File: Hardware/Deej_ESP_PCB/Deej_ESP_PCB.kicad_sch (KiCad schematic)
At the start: 1 part, among them U1 ESP32-S3-MINI-1U

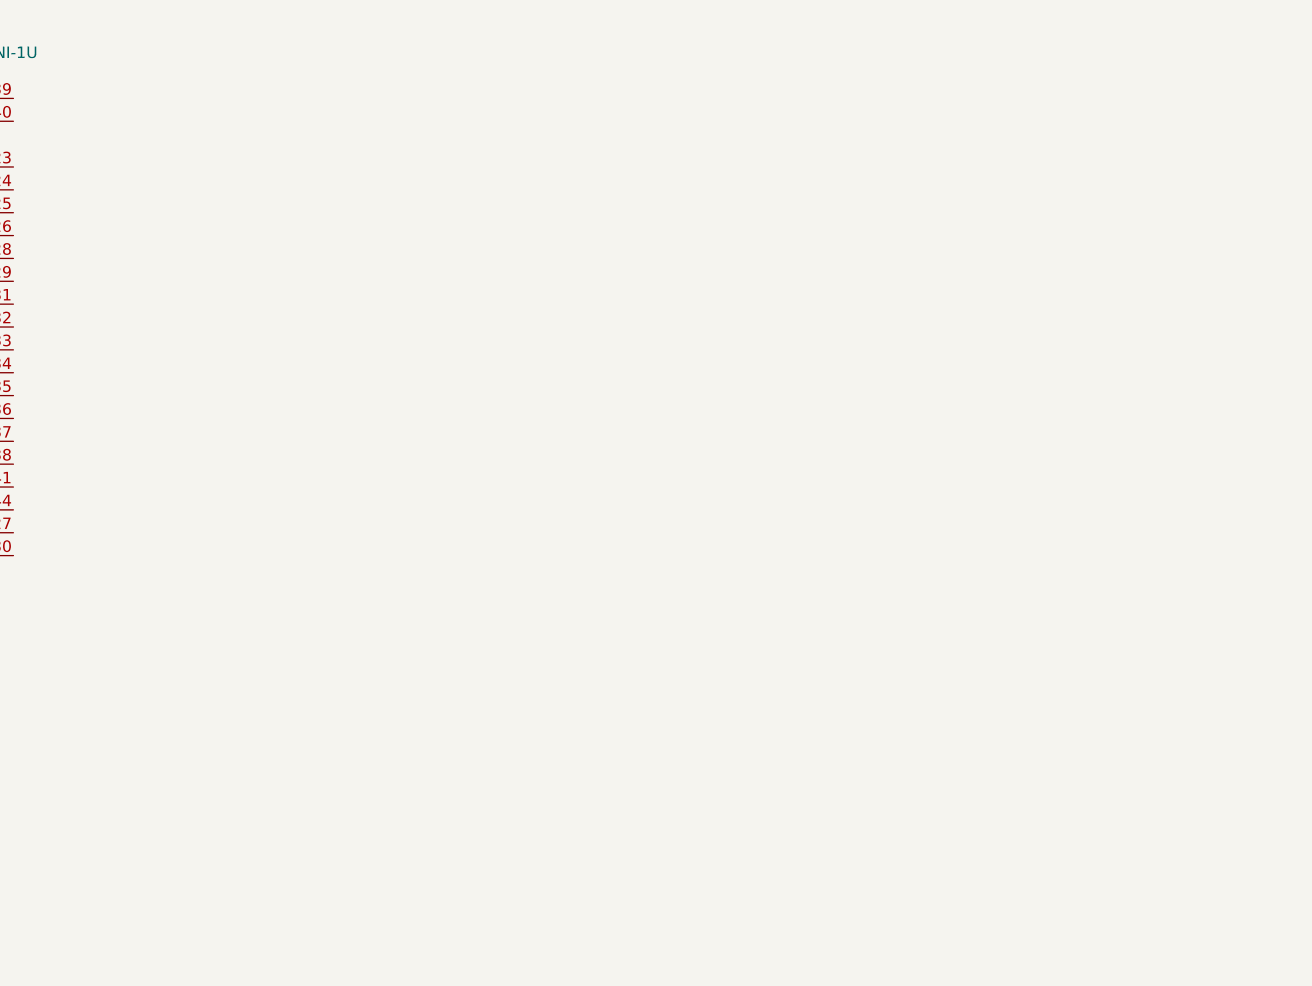
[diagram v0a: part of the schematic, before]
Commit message: Adding components to the part library
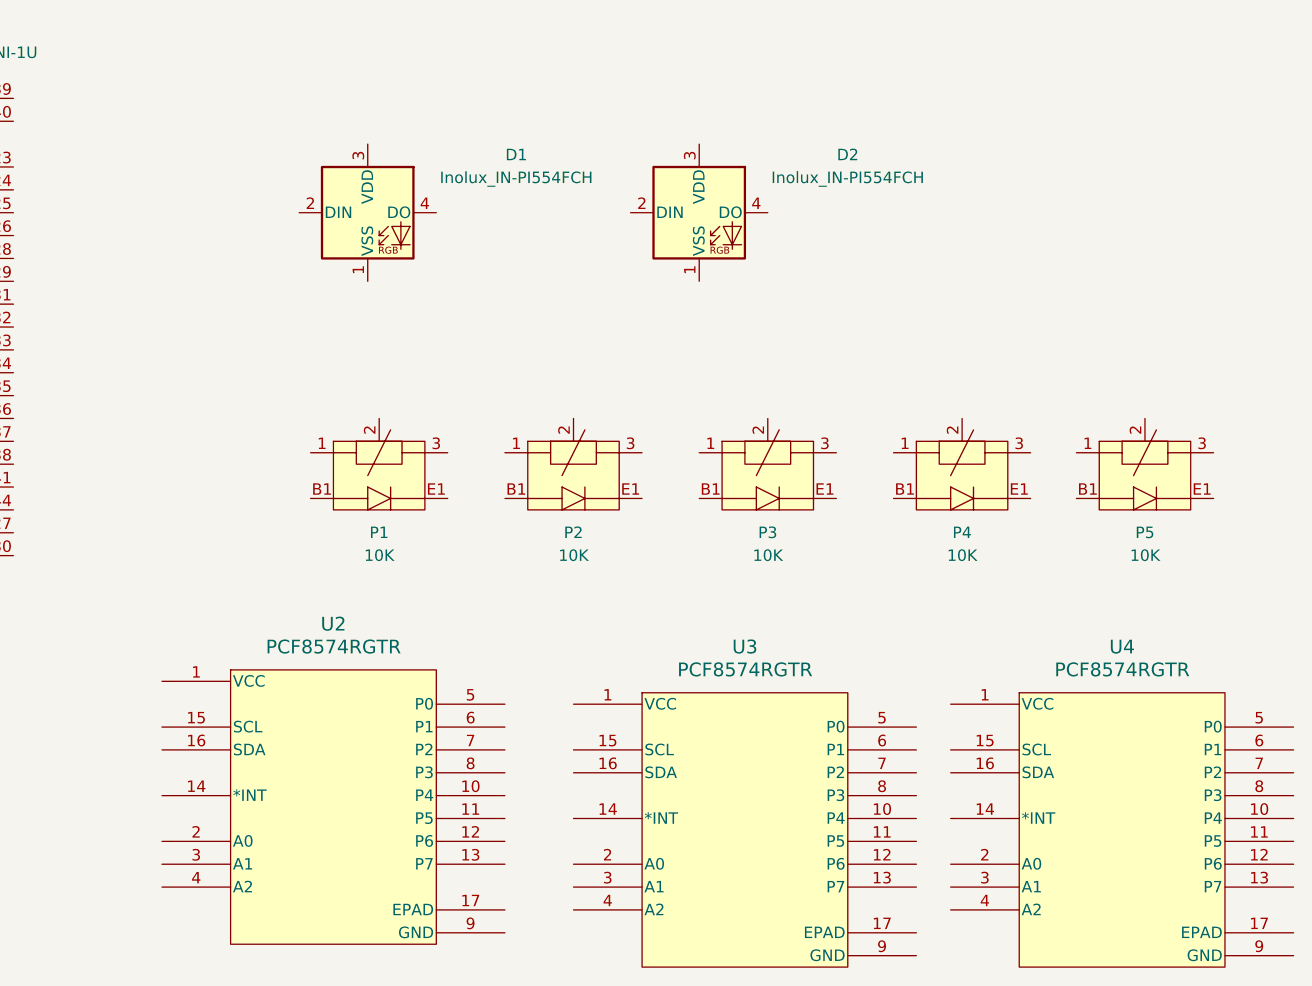
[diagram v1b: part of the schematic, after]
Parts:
- added D1, D2: Inolux_IN-PI554FCH, LED_SMD:LED_Inolux_IN-PI554FCH_PLCC4_5.0x5.0mm_P3.2mm, symbol LED:Inolux_IN-PI554FCH
- added P1, P2, P3, P4, P5: 10K, Bourns_Potentiometer:PTL01, symbol Bourns_Potentiometer:PTL01-15R0-103B1
- added U2, U3, U4: PCF8574RGTR, RGT16_1P6X1P6, symbol TI:PCF8574RGTR

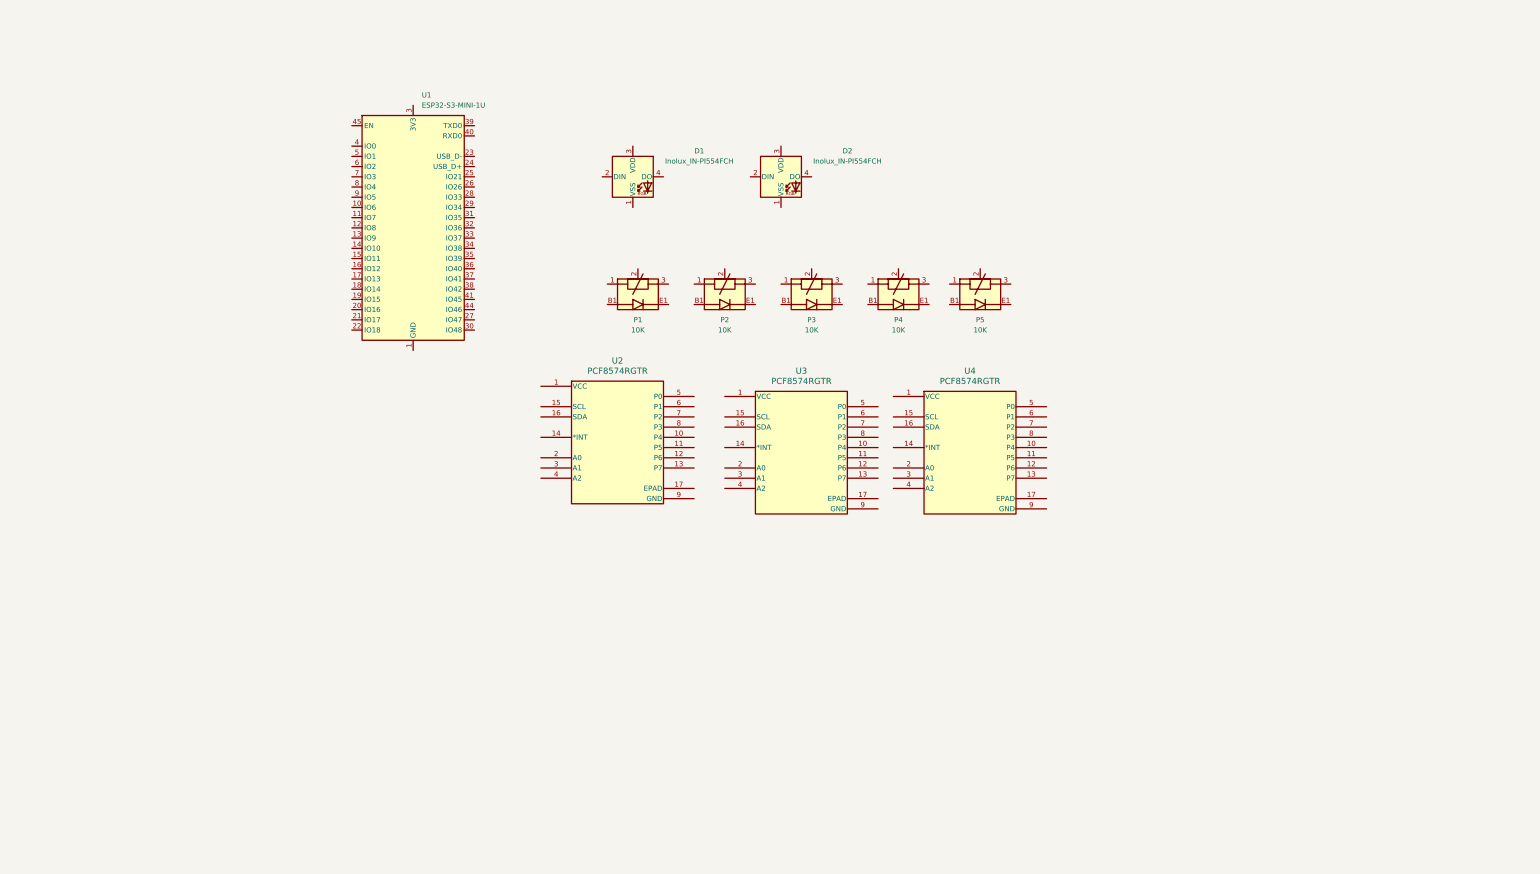
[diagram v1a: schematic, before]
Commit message: Figured out componentes for hardware debouncing and making sure all components have 3D models for when it comes time to make an enclosure
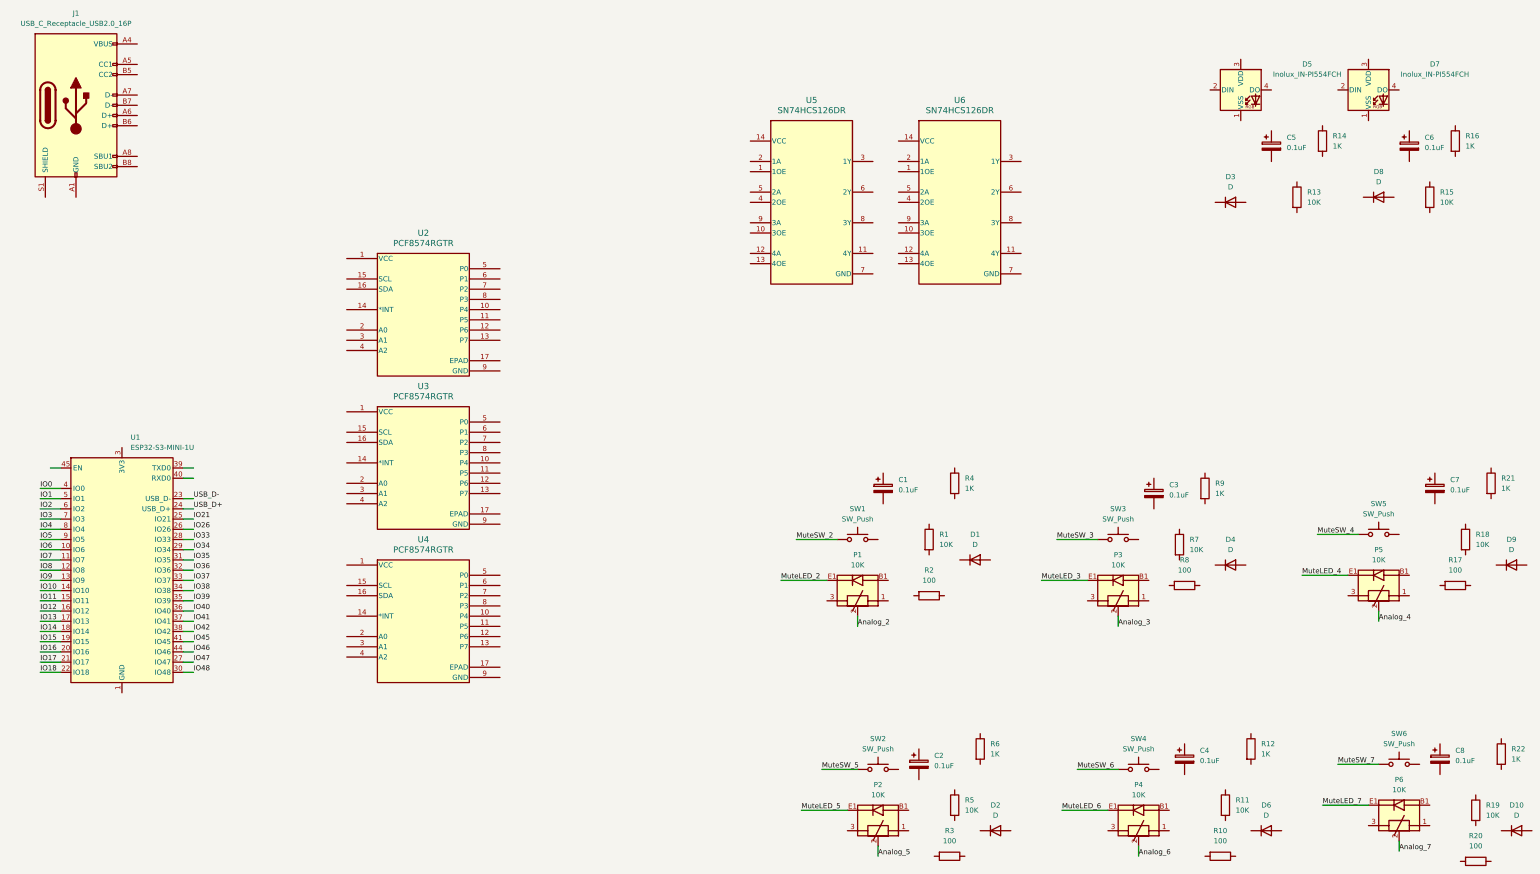
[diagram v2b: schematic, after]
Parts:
- added C1, C2, C3, C4, C5, C6, C7, C8: 0.1uF, Capacitor_Tantalum_SMD:CP_EIA-3216-18_Kemet-A_HandSolder, symbol Device:C_Polarized
- added D1, D10, D2, D3, D4, D6, D8, D9: D, Diode_SMD:D_SOD-123, symbol Device:D
- added J1: USB_C_Receptacle_USB2.0_16P, Connector_USB:USB_C_Receptacle_GCT_USB4085, symbol Connector:USB_C_Receptacle_USB2.0_16P
- added P6: 10K, Bourns_Potentiometer:PTL01, symbol Bourns_Potentiometer:PTL01-15R0-103B1
- added R1, R11, R13, R15, R18, R19, R5, R7: 10K, PCM_Resistor_SMD_AKL:R_0201_0603Metric_Pad0.64x0.40mm_HandSolder, symbol Device:R
- added R10, R17, R2, R20, R3, R8: 100, PCM_Resistor_SMD_AKL:R_0201_0603Metric_Pad0.64x0.40mm_HandSolder, symbol Device:R
- added R12, R14, R16, R21, R22, R4, R6, R9: 1K, PCM_Resistor_SMD_AKL:R_0201_0603Metric_Pad0.64x0.40mm_HandSolder, symbol Device:R
- added SW1, SW2, SW3, SW4, SW5, SW6: SW_Push, PCM_Switch_Keyboard_Cherry_MX:SW_Cherry_MX_PCB, symbol Switch:SW_Push
- added U5, U6: SN74HCS126DR, D0014A-IPC_A, symbol TI:SN74HCS126DR
- renumbered D1 to D5, D2 to D7, P4 to P2, P2 to P3, P5 to P4, P3 to P5
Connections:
- net Analog_3: now reaches P3.2
- net MuteLED_3: now reaches P3.E1
- net Analog_5: now reaches P2.2
- net MuteLED_5: now reaches P2.E1
- net at P2.L1: now also C2.2
- net Analog_6: now reaches P4.2
- net MuteLED_6: now reaches P4.E1
- net Analog_4: now reaches P5.2
- net MuteLED_4: now reaches P5.E1
- net Analog_2: now reaches P1.2
- net MuteLED_2: now reaches P1.E1
- net IO6: now reaches U1.10 (IO6)
- net IO7: now reaches U1.11 (IO7)
- net IO8: now reaches U1.12 (IO8)
- net IO9: now reaches U1.13 (IO9)
- net IO10: now reaches U1.14 (IO10)
- net IO11: now reaches U1.15 (IO11)
- net IO12: now reaches U1.16 (IO12)
- net IO13: now reaches U1.17 (IO13)
- net IO14: now reaches U1.18 (IO14)
- net IO15: now reaches U1.19 (IO15)
- net IO16: now reaches U1.20 (IO16)
- net IO17: now reaches U1.21 (IO17)
- net IO18: now reaches U1.22 (IO18)
- net USB_D-: now reaches U1.23 (USB_D-)
- net USB_D+: now reaches U1.24 (USB_D+)
- net IO21: now reaches U1.25 (IO21)
- net IO26: now reaches U1.26 (IO26)
- net IO47: now reaches U1.27 (IO47)
- net IO33: now reaches U1.28 (IO33)
- net IO34: now reaches U1.29 (IO34)
- net IO48: now reaches U1.30 (IO48)
- net IO35: now reaches U1.31 (IO35)
- net IO36: now reaches U1.32 (IO36)
- net IO37: now reaches U1.33 (IO37)
- net IO38: now reaches U1.34 (IO38)
- net IO39: now reaches U1.35 (IO39)
- net IO40: now reaches U1.36 (IO40)
- net IO41: now reaches U1.37 (IO41)
- net IO42: now reaches U1.38 (IO42)
- net IO0: now reaches U1.4 (IO0)
- net IO45: now reaches U1.41 (IO45)
- net IO46: now reaches U1.44 (IO46)
- net IO1: now reaches U1.5 (IO1)
- net IO2: now reaches U1.6 (IO2)
- net IO3: now reaches U1.7 (IO3)
- net IO4: now reaches U1.8 (IO4)
- net IO5: now reaches U1.9 (IO5)
- new net: C8.2, P6.L1
- new net: J1.A1 (GND), J1.A12 (GND), J1.B1 (GND), J1.B12 (GND)
- new net: J1.A4 (VBUS), J1.A9 (VBUS), J1.B4 (VBUS), J1.B9 (VBUS)
- new net Analog_7: P6.2
- new net MuteLED_7: P6.E1
- new net MuteSW_2: SW1.1
- new net MuteSW_3: SW3.1
- new net MuteSW_4: SW5.1
- new net MuteSW_5: SW2.1
- new net MuteSW_6: SW4.1
- new net MuteSW_7: SW6.1
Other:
- moved on the sheet: D5, D7, P1, P2, P3, P4, P5, U1, U2, U3, U4

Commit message: 3D File, ESD, and Old File Clean up
* Added the 3D files for the rotary potentiometer with switch.
* Started adding ESD diodes to components the user will touch regularly.
* Removed old files that won't be used.
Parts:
- added C10, C9: 0.1uF, Capacitor_SMD:C_0603_1608Metric_Pad1.08x0.95mm_HandSolder, symbol Device:C
- added C11, C12, C13, C14, C15, C16, C17, C18, C19, C20, C21, C22, C23, C24: 0.1uF, Capacitor_SMD:C_0201_0603Metric_Pad0.64x0.40mm_HandSolder, symbol Device:C
- added CR1, CR10, CR11, CR12, CR13, CR14, CR15, CR16, CR2, CR3, CR4, CR5, CR6, CR7, CR8, CR9: ESDALC6V1-1U2, DIODE_ESDALC6V1-1U2_STM, symbol STM:ESDALC6V1-1U2
- added D11, D12, D13, D14, D15, D16, D17, D18, D19, D20, D21, D22: Inolux_IN-PI554FCH, LED_SMD:LED_Inolux_IN-PI554FCH_PLCC4_5.0x5.0mm_P3.2mm, symbol LED:Inolux_IN-PI554FCH
- added R23, R24: 499, PCM_Resistor_SMD_AKL:R_0201_0603Metric_Pad0.64x0.40mm_HandSolder, symbol Device:R
- added U10, U7, U8, U9: 0.96" 128x64 OLED, symbol Adafruit:0_96_128x16_OLED_Module
- added U11: ECMF02-2AMX6, Package_DFN_QFN:ST_UQFN-6L_1.5x1.7mm_P0.5mm, symbol Power_Protection:ECMF02-2AMX6
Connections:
- net Analog_2: now also CR11.1
- net Analog_3: now also CR12.1
- net Analog_4: now also CR13.1
- net Analog_5: now also CR14.1
- net Analog_6: now also CR15.1
- net Analog_7: now also CR16.1
- net MuteLED_2: now also U4.5 (P0)
- net MuteLED_3: now also U4.6 (P1)
- net MuteLED_4: now also U4.7 (P2)
- net MuteLED_5: now also U4.8 (P3)
- net MuteLED_6: now also U4.10 (P4)
- net MuteLED_7: now also U4.11 (P5)
- net MuteSW_2: now also U2.7 (P2), U5.8 (3Y); no longer SW1.1
- net MuteSW_3: now also U2.8 (P3), U5.11 (4Y); no longer SW3.1
- net MuteSW_4: now also U2.10 (P4), U6.3 (1Y); no longer SW5.1
- net MuteSW_5: now also U2.11 (P5), U6.6 (2Y); no longer SW2.1
- net MuteSW_6: now also U2.12 (P6), U6.8 (3Y); no longer SW4.1
- net MuteSW_7: now also U2.13 (P7), U6.11 (4Y); no longer SW6.1
- net +3.3V: now reaches R8.1
- net +3.3V: now also P1.1, P2.1, P3.1, P4.1, P5.1, P6.1, R1.1, R10.1, R11.1, R17.1, R18.1, R19.1, R2.1, R20.1, R3.1, R5.1, R7.1, U6.1 (1OE), U6.10 (3OE), U6.13 (4OE), U6.14 (VCC), U6.4 (2OE), C10.2, C9.2, U10.6 (3V3), U7.6 (3V3), U8.6 (3V3), U9.6 (3V3)
- net at R8.2: now also P3.B1
- net at R5.2: now also D2.2 (A), R6.1, SW2.2
- net GND: now reaches P3.3
- net GND: now also C2.2, C4.2, C7.2, C8.2, D5.1 (VSS), D7.1 (VSS), P1.3, P2.3, P4.3, P5.3, P6.3, SW2.1, SW4.1, SW5.1, SW6.1, U5.7 (GND), U6.7 (GND), C10.1, C11.2, C12.2, C13.2, C14.2, C15.2, C16.2, C17.2, C18.2, C19.2, C20.2, C21.2, C22.2, C23.2, C24.2, C9.1, CR1.2, CR11.2, CR12.2, CR13.2, CR14.2, CR15.2, CR16.2, CR2.2, CR3.2, CR4.2, D11.1 (VSS), D12.1 (VSS), D13.1 (VSS), D14.1 (VSS), D15.1 (VSS), D16.1 (VSS), D17.1 (VSS), D18.1 (VSS), D19.1 (VSS), D20.1 (VSS), D21.1 (VSS), D22.1 (VSS), U10.8 (GND), U7.8 (GND), U8.8 (GND), U9.8 (GND)
- net at SW1.2: now also D1.2 (A), R1.2, R4.1
- net at R2.2: now also P1.B1
- net at P2.B1: now also R3.2
- net at P2.L1: no longer C2.2
- net at R10.2: now also P4.B1
- net at R9.1: now also D4.2 (A), R7.2, SW3.2
- net at R9.2: now also C3.1, D4.1 (K), CR5.1
- net at D1.1 (K): now also C1.1, R4.2, CR6.1
- net at D2.1 (K): now also C2.1, R6.2, U6.5 (2A), CR3.1
- net at C3.2: now also C1.2, SW1.1, SW3.1, CR5.2, CR6.2
- net at D5.2 (DIN): now also D16.4 (DO)
- net +5V: now reaches D5.3 (VDD)
- net +5V: now also D7.3 (VDD), C11.1, C12.1, C13.1, C14.1, C15.1, C16.1, C17.1, C18.1, C19.1, C20.1, C21.1, C22.1, C23.1, C24.1, D11.3 (VDD), D12.3 (VDD), D13.3 (VDD), D14.3 (VDD), D15.3 (VDD), D16.3 (VDD), D17.3 (VDD), D18.3 (VDD), D19.3 (VDD), D20.3 (VDD), D21.3 (VDD), D22.3 (VDD), U10.7 (VCC), U7.7 (VCC), U8.7 (VCC), U9.7 (VCC)
- net at D5.4 (DO): now also D17.2 (DIN)
- net at U6.12 (4A): now also C8.1, D10.1 (K), R22.2, CR1.1
- net at U6.2 (1A): now also C7.1, D9.1 (K), R21.2, CR4.1
- net at U6.9 (3A): now also C4.1, D6.1 (K), R12.2, CR2.1
- net MuteSW_0: now reaches U2.5 (P0)
- net MuteSW_0: now also U5.3 (1Y)
- net MuteSW_1: now reaches U2.6 (P1)
- net MuteSW_1: now also U5.6 (2Y)
- net at R20.2: now also P6.B1
- net at R19.2: now also D10.2 (A), R22.1, SW6.2
- net at D6.2 (A): now also R11.2, R12.1, SW4.2
- net at D7.2 (DIN): now also D22.4 (DO)
- net at D7.4 (DO): now also R24.1
- net at D9.2 (A): now also R18.2, R21.1, SW5.2
- net at R17.2: now also P5.B1
- net at P6.L1: no longer C8.2
- net at J1.A6 (D+): now also J1.B6 (D+), U11.1 (D+_in)
- net at J1.A7 (D-): now also J1.B7 (D-), U11.2 (D-_in)
- new net: D11.4 (DO), D12.2 (DIN)
- new net: D12.4 (DO), D13.2 (DIN)
- new net: D19.4 (DO), D20.2 (DIN)
- new net: D20.4 (DO), D21.2 (DIN)
- new net: D21.4 (DO), D22.2 (DIN)
- new net: D13.4 (DO), D14.2 (DIN)
- new net: D17.4 (DO), D18.2 (DIN)
- new net: D18.4 (DO), D19.2 (DIN)
- new net: D11.2 (DIN), R23.2
- new net: D14.4 (DO), D15.2 (DIN)
- new net: D15.4 (DO), D16.2 (DIN)
- new net CS0: U8.5 (CS)
- new net CS1: U7.5 (CS)
- new net CS2: U10.5 (CS)
- new net CS3: U9.5 (CS)
- new net D/C: U10.3 (D/C), U7.3 (D/C), U8.3 (D/C), U9.3 (D/C)
- new net MOSI: U10.1 (MOSI), U7.1 (MOSI), U8.1 (MOSI), U9.1 (MOSI)
- new net NEOLED: R23.1
- new net RST: U10.4 (RST), U7.4 (RST), U8.4 (RST), U9.4 (RST)
- new net SCLK: U10.2 (SCLK), U7.2 (SCLK), U8.2 (SCLK), U9.2 (SCLK)
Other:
- moved on the sheet: C1, C2, C3, C4, C5, C6, C7, C8, D1, D10, D2, D3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
